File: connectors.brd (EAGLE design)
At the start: 14.5 x 14.5 mm, 19 parts, among them CON2 PINHEAD_1X03-2.54-RA, CON3 CON-4P-JST_GH-RA, CON4 PINHEAD_1X02-2, CON5 PINHEAD_1X02-2, CON6 PINHEAD_1X07-2, CON8 CON-4P-JST_GH-RA, IC1 TPD3S014DBVR-SOT23-6, IC3 TJA1051

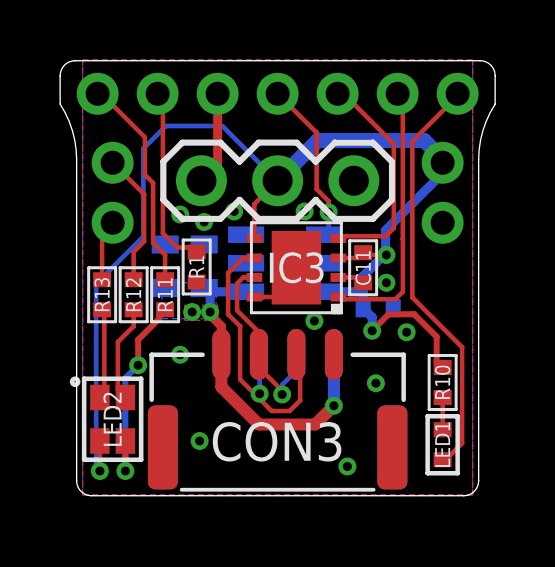
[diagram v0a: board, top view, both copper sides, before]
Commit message: pinout fixes
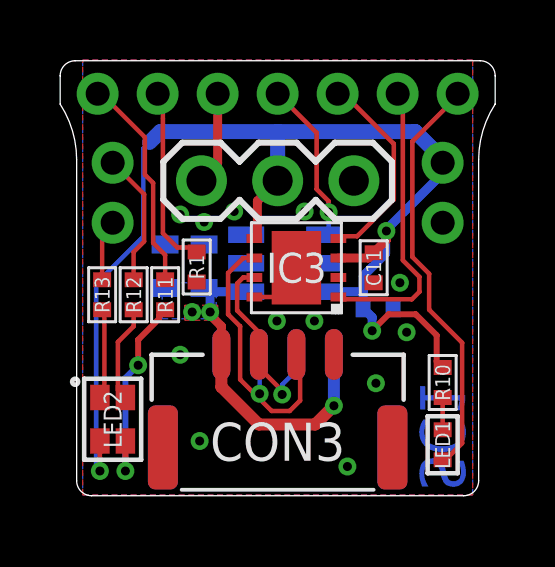
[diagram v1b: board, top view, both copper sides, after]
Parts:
- moved C11 0.35 mm to (3.20, 5.10)
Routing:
- net VDD_5V: track 40.4 -> 41.8 mm
- net GND: track 2.64 -> 1.74 mm, vias 11 -> 12
- net CAN1_TX: track 8.96 -> 9.74 mm
- net CAN1_RX: track 7.36 -> 6.80 mm
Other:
- board text added: "SC1"
